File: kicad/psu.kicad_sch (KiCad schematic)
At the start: 4 parts

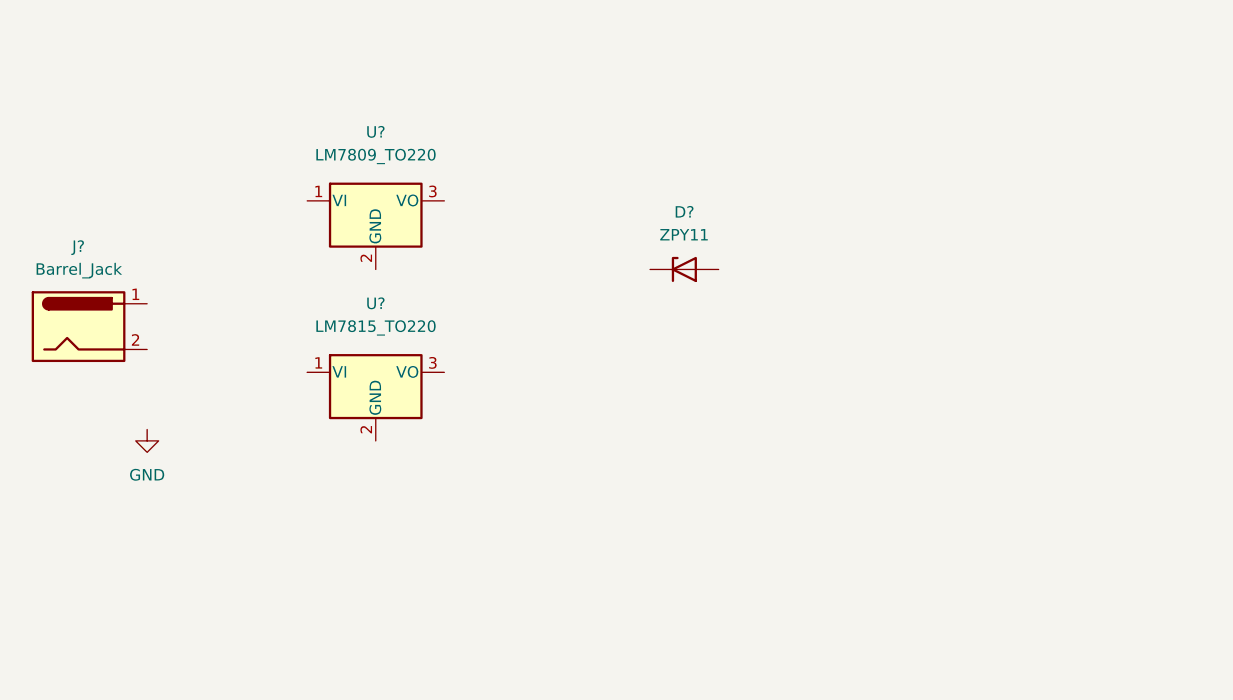
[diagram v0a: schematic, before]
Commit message: Schematic: added some wiring and a voltage divider 15 V --> 12.68 V
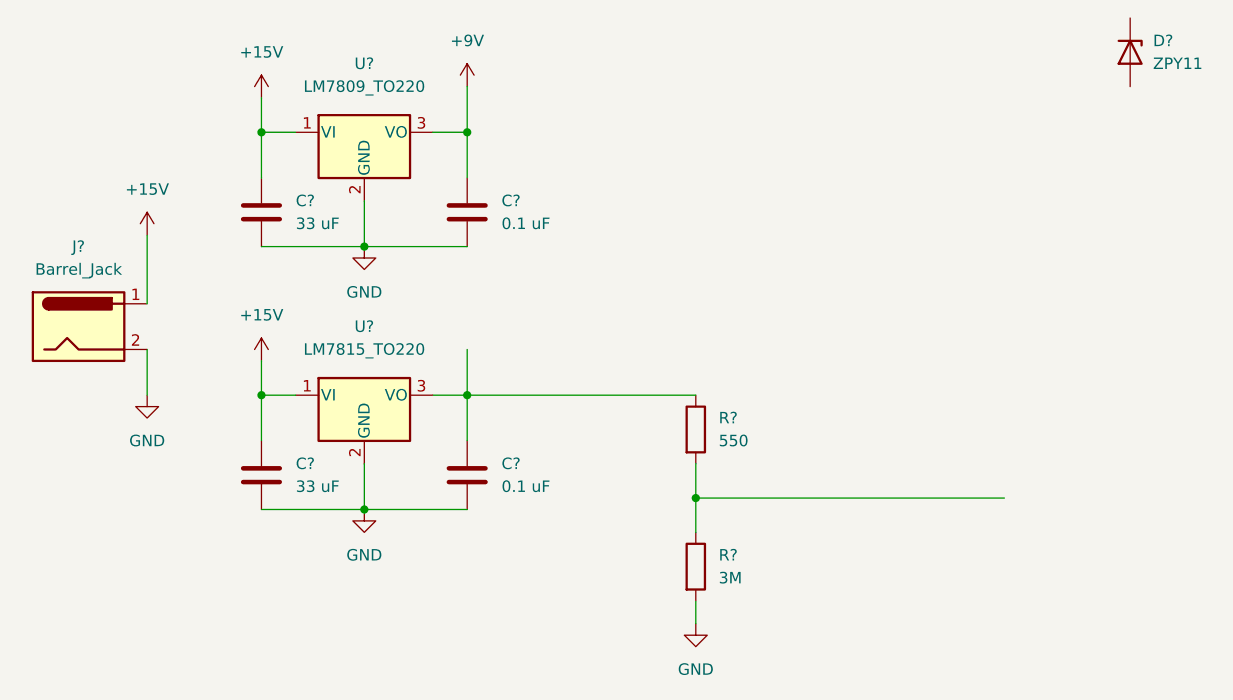
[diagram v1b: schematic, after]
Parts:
- added C? (x2): 33 uF, symbol Device:C
- added C? (x2): 0.1 uF, symbol Device:C
- added R?: 3M, symbol Device:R
- added R?: 550, symbol Device:R
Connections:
- net GND: now also J?.2, U?.2 (GND), U?.2 (GND), C?.2, C?.2, C?.2, C?.2, R?.2
- net +15V: now reaches U?.1 (VI)
- net +15V: now also J?.1, U?.1 (VI), C?.1, C?.1
- net at U?.3 (VO): now also C?.1, R?.1
- net +9V: now reaches U?.3 (VO)
- net +9V: now also C?.1
- new net: R?.1, R?.2
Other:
- moved on the sheet: D?, U?
